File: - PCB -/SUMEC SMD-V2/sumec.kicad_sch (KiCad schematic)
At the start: 2 parts

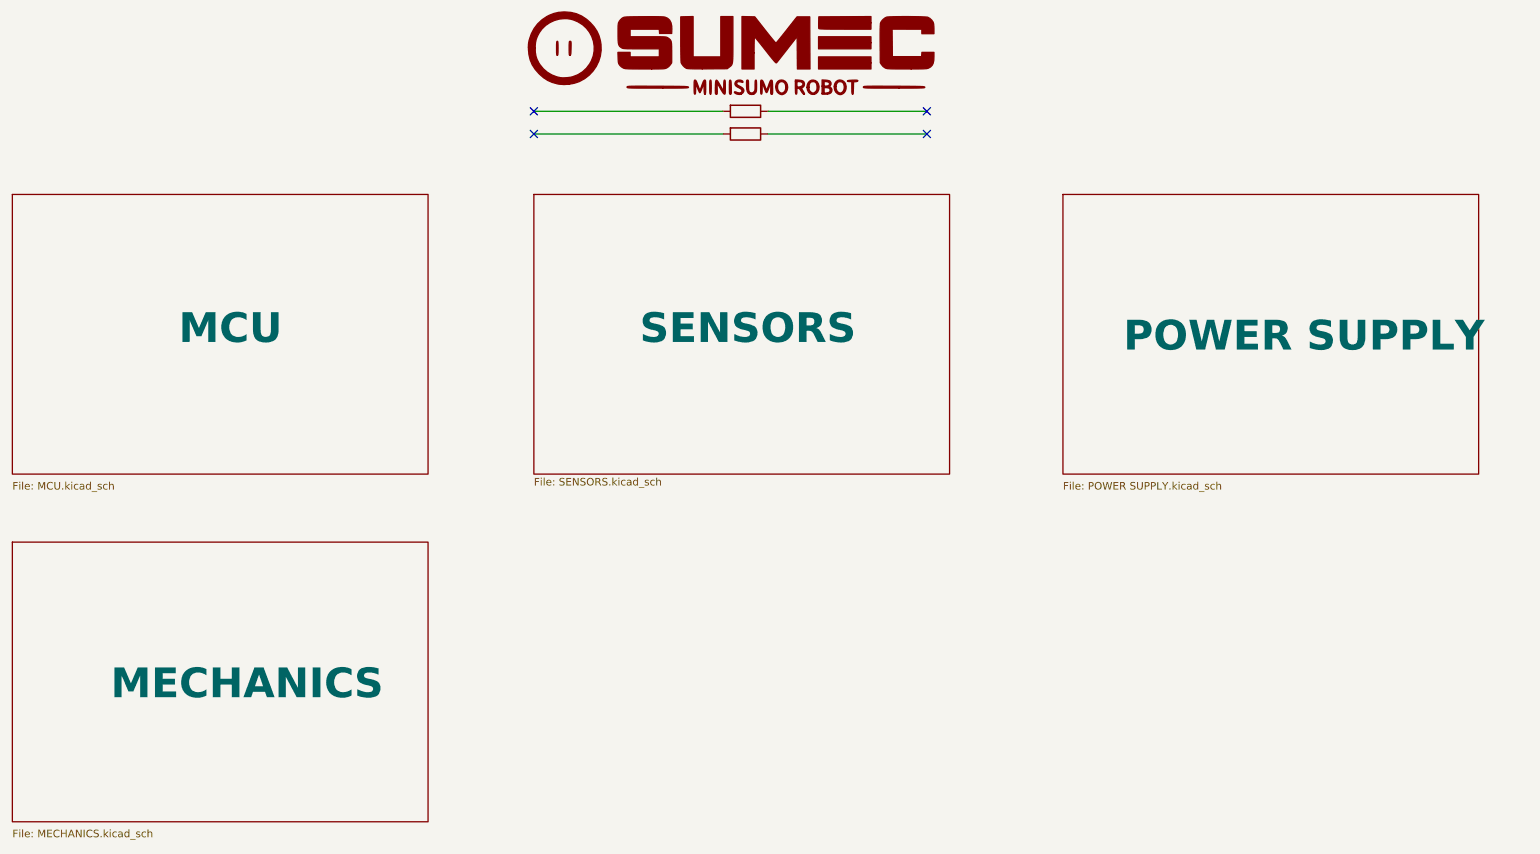
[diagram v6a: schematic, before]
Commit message: Revert "mateji co jsi kurva delal v slozce PCB??"
This reverts commit db6b80f6998ca08dcf5bbaff0895d0cea7c46a95.
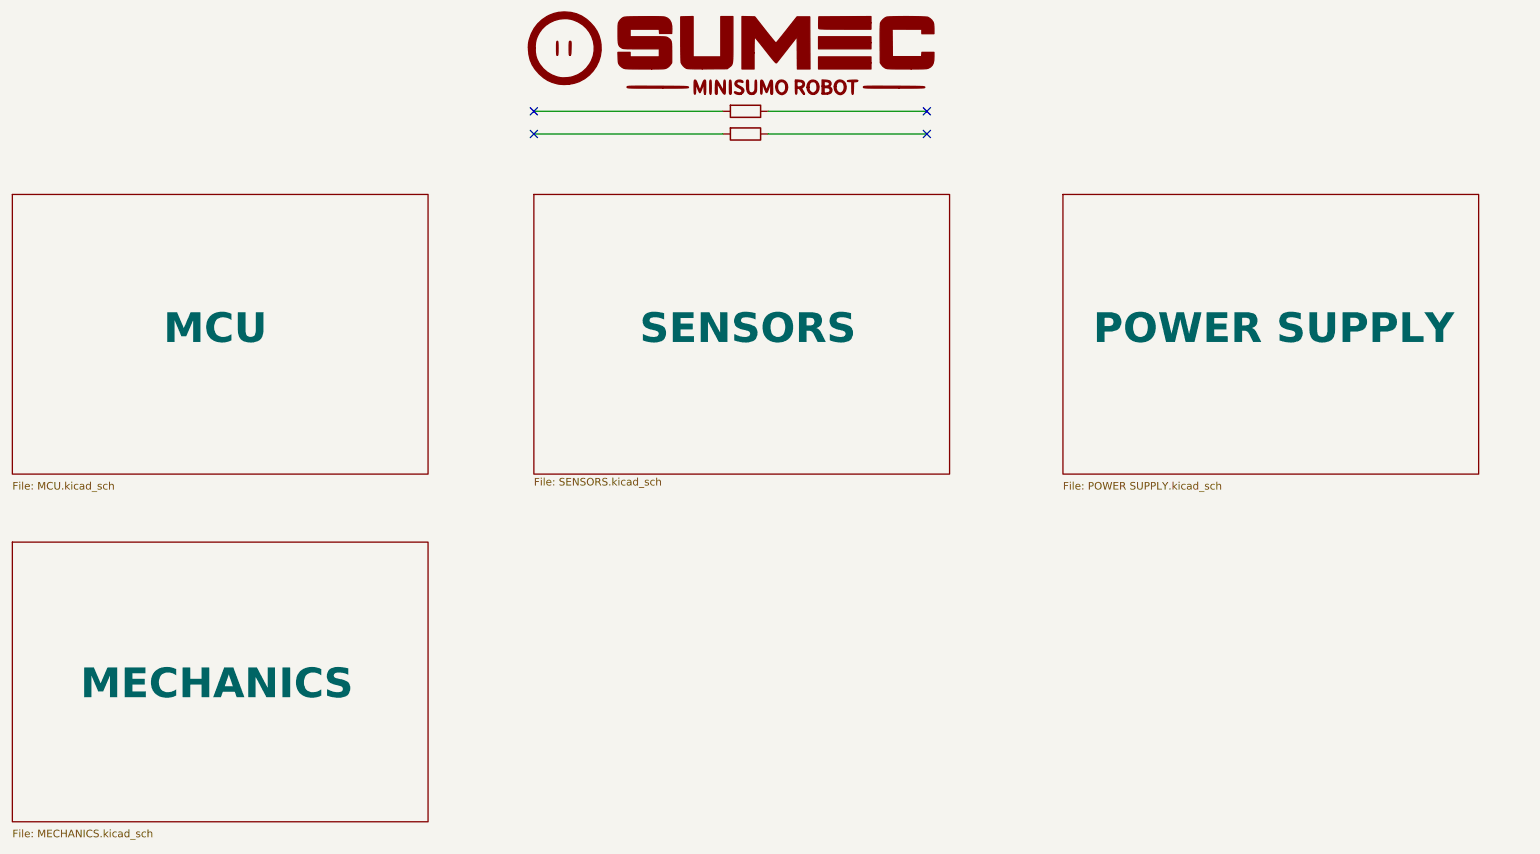
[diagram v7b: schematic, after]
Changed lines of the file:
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@@
     (in_bom yes) (on_board yes) (dnp no) (fields_autoplaced)
     (property "Reference" "R3" (at 151.13 39.37 90)
-      (effects (font (face "Bahnschrift") (size 1.27 1.27)) hide)
+      (effects (font (size 1.27 1.27)) hide)
     )
     (property "Value" "R" (at 151.13 36.83 90)
-      (effects (font (face "Bahnschrift") (size 1.27 1.27)) hide)
+      (effects (font (size 1.27 1.27)) hide)
     )
     (property "Footprint" "sumec-smdV2_library:R2D2" (at 151.13 32.512 90)
-      (effects (font (face "Bahnschrift") (size 1.27 1.27)) hide)
+      (effects (font (size 1.27 1.27)) hide)
     )
     (property "Datasheet" "~" (at 151.13 34.29 0)
-      (effects (font (face "Bahnschrift") (size 1.27 1.27)) hide)
+      (effects (font (size 1.27 1.27)) hide)
     )
     (pin "1")
@@
     (in_bom yes) (on_board yes) (dnp no) (fields_autoplaced)
     (property "Reference" "R8" (at 151.13 43.18 90)
-      (effects (font (face "Bahnschrift") (size 1.27 1.27)) hide)
+      (effects (font (size 1.27 1.27)) hide)
     )
     (property "Value" "R" (at 151.13 40.64 90)
-      (effects (font (face "Bahnschrift") (size 1.27 1.27)) hide)
+      (effects (font (size 1.27 1.27)) hide)
     )
     (property "Footprint" "sumec-smdV2_library:Logo" (at 151.13 36.322 90)
-      (effects (font (face "Bahnschrift") (size 1.27 1.27)) hide)
+      (effects (font (size 1.27 1.27)) hide)
     )
     (property "Datasheet" "~" (at 151.13 38.1 0)
-      (effects (font (face "Bahnschrift") (size 1.27 1.27)) hide)
+      (effects (font (size 1.27 1.27)) hide)
     )
     (pin "1")
@@
     (in_bom yes) (on_board yes) (dnp no) (fields_autoplaced)
     (property "Reference" "#G1" (at 147.32 14.7743 0)
-      (effects (font (face "Bahnschrift") (size 1.27 1.27)) hide)
+      (effects (font (size 1.27 1.27)) hide)
     )
     (property "Value" "LOGO" (at 147.32 36.0257 0)
-      (effects (font (face "Bahnschrift") (size 1.27 1.27)) hide)
+      (effects (font (size 1.27 1.27)) hide)
     )
     (property "Footprint" "" (at 147.32 25.4 0)
-      (effects (font (face "Bahnschrift") (size 1.27 1.27)) hide)
+      (effects (font (size 1.27 1.27)) hide)
     )
     (property "Datasheet" "" (at 147.32 25.4 0)
-      (effects (font (face "Bahnschrift") (size 1.27 1.27)) hide)
+      (effects (font (size 1.27 1.27)) hide)
     )
     (instances
@@
     (stroke (width 0.1524) (type solid) (color 0 0 0 1))
     (fill (color 255 255 255 1.0000))
-    (property "Sheetname" "MECHANICS" (at 44.45 133.35 0)
-      (effects (font (face "Bahnschrift") (size 5 5) bold (color 0 0 0 1)) (justify left bottom))
+    (property "Sheetname" "MECHANICS" (at 39.37 133.35 0)
+      (effects (font (size 5 5) bold (color 0 0 0 1)) (justify left bottom))
     )
     (property "Sheetfile" "MECHANICS.kicad_sch" (at 27.94 154.94 0)
-      (effects (font (face "Bahnschrift") (size 1.27 1.27) (color 0 0 0 1)) (justify left top))
+      (effects (font (size 1.27 1.27) (color 0 0 0 1)) (justify left top))
     )
     (instances
@@
     (stroke (width 0.1524) (type solid) (color 0 0 0 1))
     (fill (color 255 255 255 1.0000))
-    (property "Sheetname" "MCU" (at 55.88 73.66 0)
-      (effects (font (face "Bahnschrift") (size 5 5) bold (color 0 0 0 1)) (justify left bottom))
+    (property "Sheetname" "MCU" (at 53.34 73.66 0)
+      (effects (font (size 5 5) bold (color 0 0 0 1)) (justify left bottom))
     )
     (property "Sheetfile" "MCU.kicad_sch" (at 27.94 96.52 0)
-      (effects (font (face "Bahnschrift") (size 1.27 1.27) (color 0 0 0 1)) (justify left top))
+      (effects (font (size 1.27 1.27) (color 0 0 0 1)) (justify left top))
     )
     (instances
@@
     (stroke (width 0.1524) (type solid) (color 0 0 0 1))
     (fill (color 255 255 255 1.0000))
-    (property "Sheetname" "POWER SUPPLY" (at 214.63 74.93 0)
-      (effects (font (face "Bahnschrift") (size 5 5) bold (color 0 0 0 1)) (justify left bottom))
+    (property "Sheetname" "POWER SUPPLY" (at 209.55 73.66 0)
+      (effects (font (size 5 5) bold (color 0 0 0 1)) (justify left bottom))
     )
     (property "Sheetfile" "POWER SUPPLY.kicad_sch" (at 204.47 96.52 0)
-      (effects (font (face "Bahnschrift") (size 1.27 1.27) (color 0 0 0 1)) (justify left top))
+      (effects (font (size 1.27 1.27) (color 0 0 0 1)) (justify left top))
     )
     (instances
@@
     (fill (color 255 255 255 1.0000))
     (property "Sheetname" "SENSORS" (at 133.35 73.66 0)
-      (effects (font (face "Bahnschrift") (size 5 5) bold (color 0 0 0 1)) (justify left bottom))
+      (effects (font (size 5 5) bold (color 0 0 0 1)) (justify left bottom))
     )
     (property "Sheetfile" "SENSORS.kicad_sch" (at 115.57 95.8346 0)
-      (effects (font (face "Bahnschrift") (size 1.27 1.27) (color 0 0 0 1)) (justify left top))
+      (effects (font (size 1.27 1.27) (color 0 0 0 1)) (justify left top))
     )
     (property "Field2" "" (at 115.57 48.26 0)
-      (effects (font (face "Bahnschrift") (size 1.27 1.27)) hide)
+      (effects (font (size 1.27 1.27)) hide)
     )
     (instances
